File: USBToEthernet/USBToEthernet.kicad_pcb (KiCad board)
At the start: 4 copper layers, 52.4 x 25.3 mm, 54 parts, among them J1 0480372200, J2 L836-1J1T-43, SW1 SW_Push, U1 LAN7500-ABJZ, U2 NCP1117-3.3_SOT223, U3 93LCxxAxxOT, U4 USBLC6-2SC6, U6 AMS1117-1.2, Y1 25Mhz

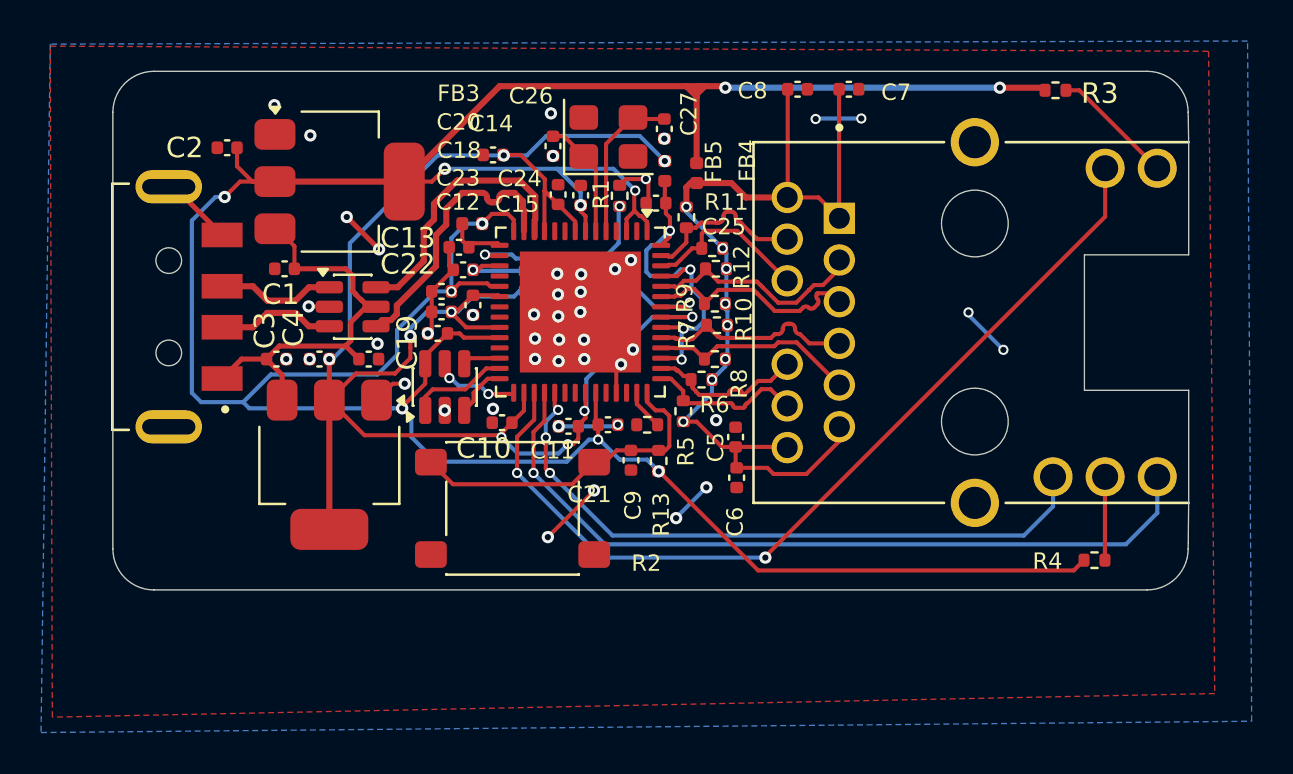
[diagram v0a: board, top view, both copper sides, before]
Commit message: Added more space between capacitors
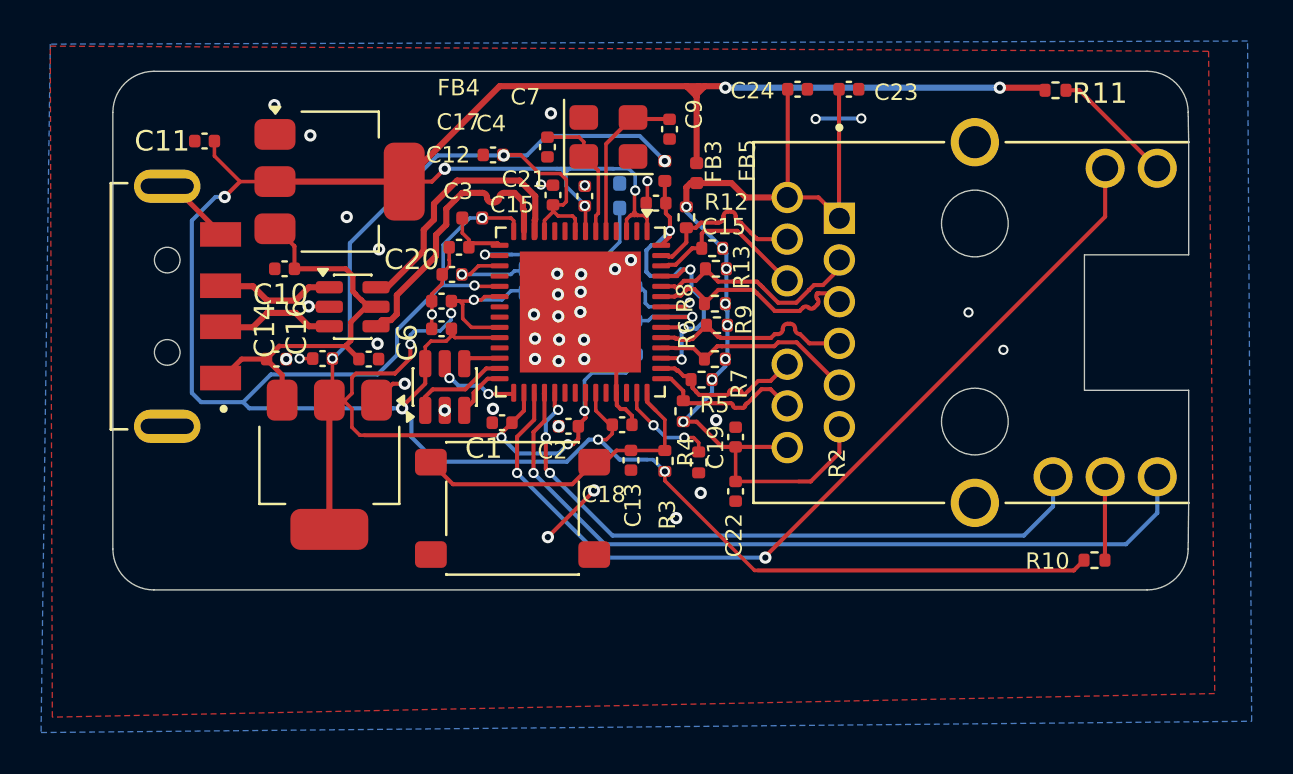
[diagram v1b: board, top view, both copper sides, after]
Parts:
- removed the C13 at (72.0, 87.8)
- removed the C23 at (70.5, 87.2)
- C5: renamed from C16; footprint Capacitor_SMD:C_0402_1005Metric -> Capacitor_SMD:C_0402_1005Metric_Pad0.74x0.62mm_HandSolder
- C8: renamed from C17; footprint Capacitor_SMD:C_0402_1005Metric -> Capacitor_SMD:C_0402_1005Metric_Pad0.74x0.62mm_HandSolder
- FB1, FB2: footprint Inductor_SMD:L_0402_1005Metric -> Inductor_SMD:L_0402_1005Metric_Pad0.77x0.64mm_HandSolder
- R1: footprint Resistor_SMD:R_0402_1005Metric -> Resistor_SMD:R_0402_1005Metric_Pad0.72x0.64mm_HandSolder; moved to B.Cu
- moved R2 3.11 mm to (83.0, 95.5), turned to 90 degrees
- moved C11 1.15 mm to (58.9, 79.8)
- moved C5 1.13 mm to (79.4, 90.2)
- moved C18 0.69 mm to (79.3, 93.7)
- moved C22 0.67 mm to (84.8, 96.9)
- moved C12 0.59 mm to (71.0, 86.3)
- moved FB1 0.58 mm to (79.3, 88.6)
- moved C3 0.53 mm to (70.5, 87.6)
- moved R3 0.30 mm to (81.4, 95.4)
- moved C20 0.29 mm to (70.5, 89.0)
- moved FB4 0.27 mm to (72.0, 83.6)
- moved C7 0.27 mm to (75.7, 80.1)
- moved C9 0.26 mm to (81.6, 79.2)
- moved C15 0.25 mm to (75.9, 82.5)
- moved C21 0.20 mm to (77.5, 82.5)
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- renumbered C10 to C1, C1 to C10, C2 to C11, C18 to C12, C9 to C13, C3 to C14, C25 to C15, C4 to C16, C20 to C17, C21 to C18, C5 to C19, C11 to C2, C22 to C20, C24 to C21, C6 to C22, C7 to C23, C8 to C24, C12 to C3, C14 to C4, C19 to C6, C26 to C7, C27 to C9, FB5 to FB3, FB3 to FB4, FB4 to FB5, R4 to R10, R3 to R11, R11 to R12, R12 to R13, R13 to R3, R5 to R4, R6 to R5, R7 to R6, R8 to R7, R9 to R8, R10 to R9, U3 to U1, U1 to U2, U4 to U3, U2 to U4, U6 to U5
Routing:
- net GND: track 33.7 -> 23.0 mm, vias 45 -> 41
- net Net-(U2B-ETHRBIAS): track 1.98 -> 4.92 mm, vias 0 -> 2
- net +3V3: track 160.8 -> 163.5 mm
- net +1V2: track 87.6 -> 89.7 mm, vias 9 -> 10
- net /VDD12PLL: track 6.09 -> 7.60 mm
- net /VDD12USBPLL: track 3.94 -> 5.24 mm
- net /TR0: track 46.4 -> 47.5 mm
- net /XO: track 5.81 -> 6.59 mm
- net Net-(U2B-USBRBIAS): track 9.46 -> 9.28 mm, vias 2 -> 1
